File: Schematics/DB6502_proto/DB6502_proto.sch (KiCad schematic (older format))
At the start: 16 parts, among them U1 74AC32, U2 74HC21, U3 74AC74, U4 74AC04, U5 65C02S, U6 74AC08, U7 22V10C, U8 74AC138

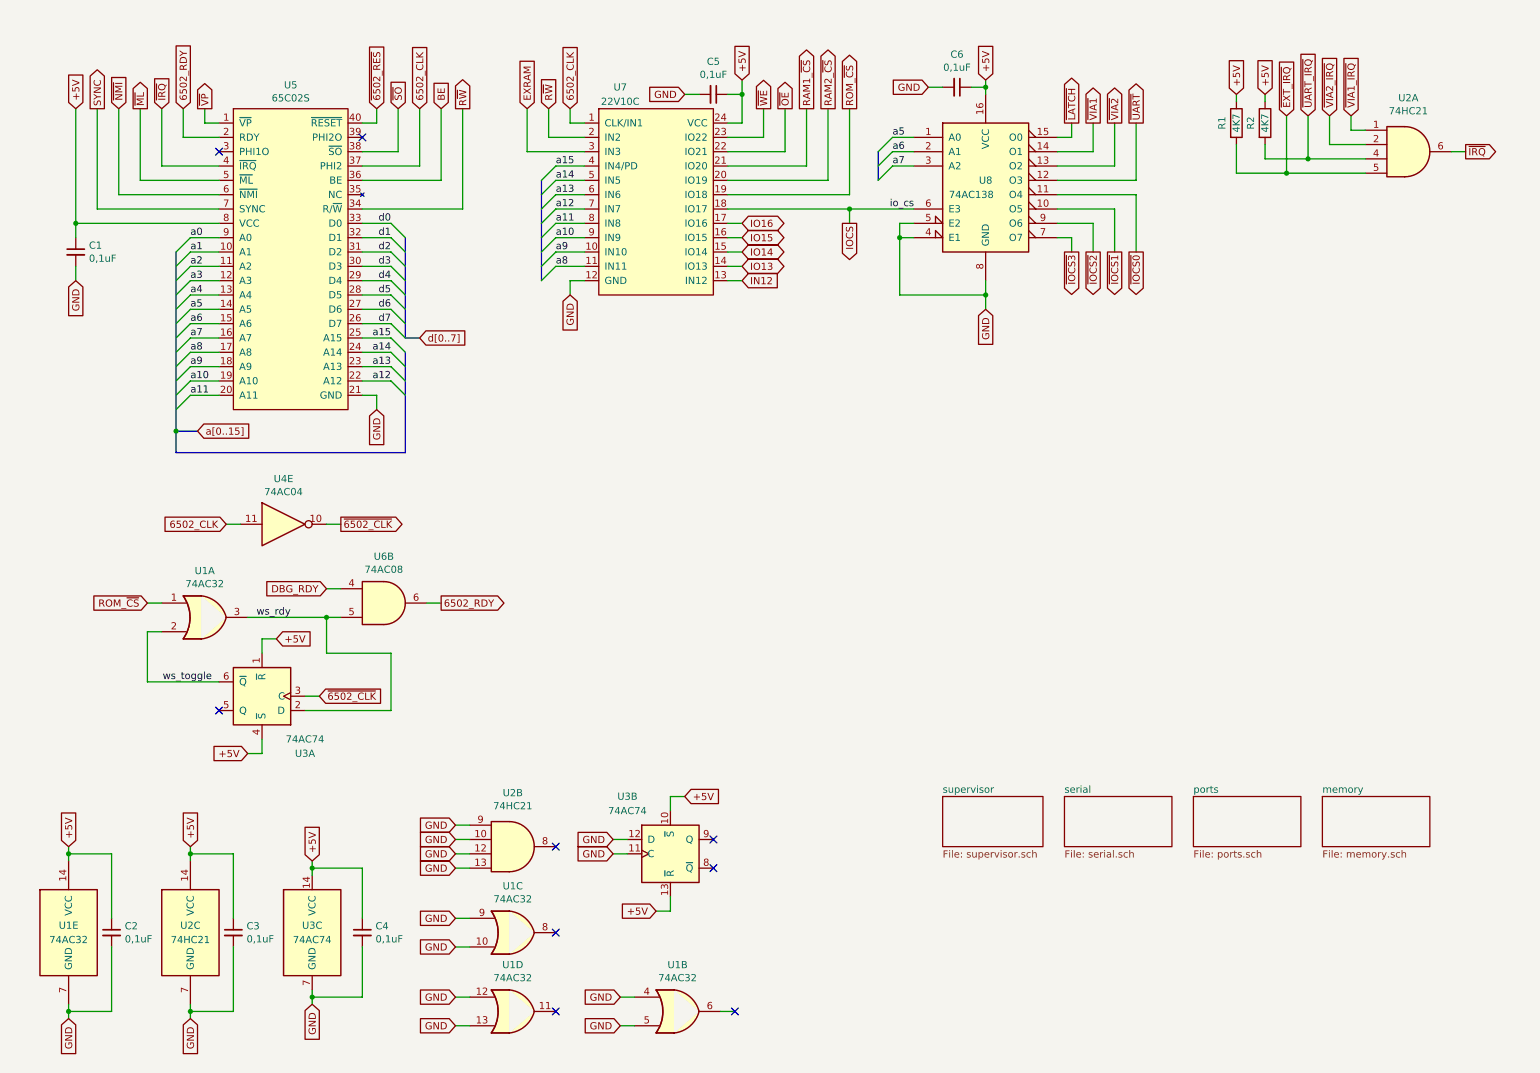
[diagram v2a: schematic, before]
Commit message: Rearranged global labels to make things neat
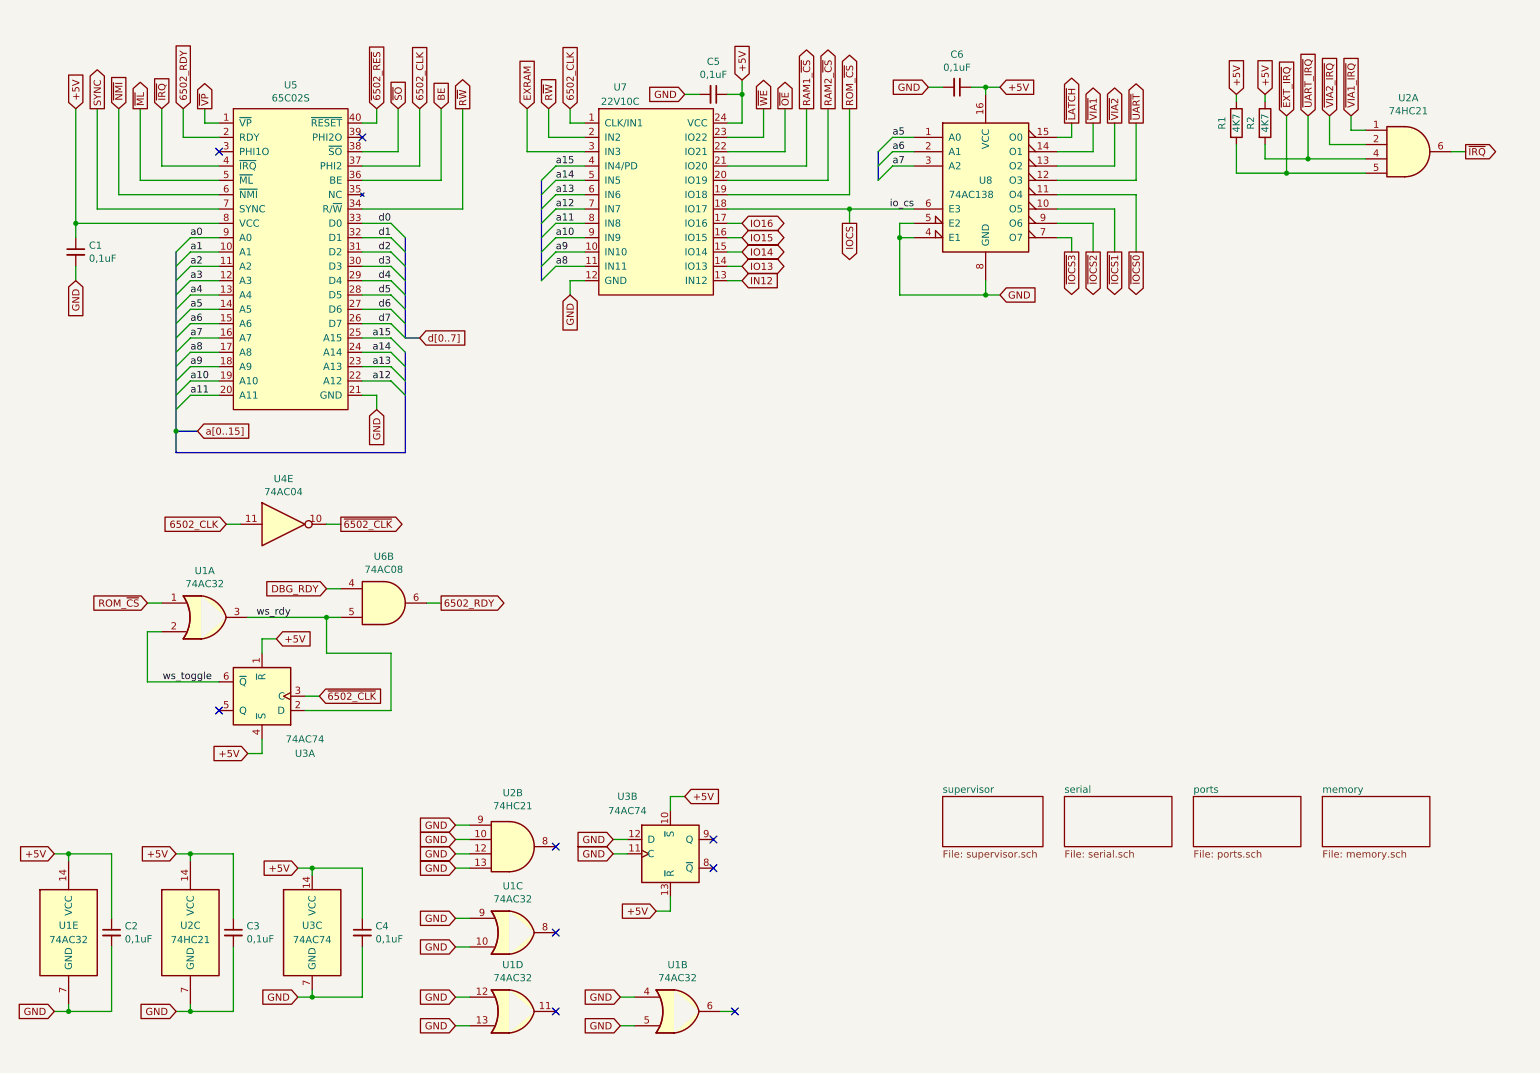
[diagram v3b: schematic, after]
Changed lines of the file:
@@
 Wire Wire Line
 	6600 1550 6750 1550
-Text GLabel 7250 950  1    50   Input ~ 0
-+5V
-Wire Wire Line
-	7250 950  7250 1000
-Text GLabel 7250 2550 3    50   Input ~ 0
-GND
-Wire Wire Line
-	7250 2550 7250 2450
+Text GLabel 7350 1000 2    50   Input ~ 0
++5V
+Wire Wire Line
+	7350 1000 7250 1000
+Text GLabel 7350 2450 2    50   Input ~ 0
+GND
+Wire Wire Line
+	7350 2450 7250 2450
 Wire Wire Line
 	7250 2450 6650 2450
@@
 	1    0    0    -1
 $EndComp
-Text GLabel 850  6300 1    50   Input ~ 0
-+5V
-Text GLabel 850  7500 3    50   Input ~ 0
-GND
-Wire Wire Line
-	850  6300 850  6350
-Wire Wire Line
-	850  7500 850  7450
+Text GLabel 750  6350 0    50   Input ~ 0
++5V
+Text GLabel 750  7450 0    50   Input ~ 0
+GND
+Wire Wire Line
+	750  6350 850  6350
+Wire Wire Line
+	750  7450 850  7450
 $Comp
 L Device:C_Small C2
@@
 	1    0    0    -1
 $EndComp
-Text GLabel 1700 6300 1    50   Input ~ 0
-+5V
-Text GLabel 1700 7500 3    50   Input ~ 0
-GND
-Wire Wire Line
-	1700 7500 1700 7450
+Text GLabel 1600 6350 0    50   Input ~ 0
++5V
+Text GLabel 1600 7450 0    50   Input ~ 0
+GND
+Wire Wire Line
+	1600 7450 1700 7450
 Wire Wire Line
 	1700 6400 1700 6350
@@
 Connection ~ 1700 6350
 Wire Wire Line
-	1700 6350 1700 6300
+	1700 6350 1600 6350
 Wire Wire Line
 	1700 7450 2000 7450
@@
 	1    0    0    -1
 $EndComp
-Text GLabel 2550 7400 3    50   Input ~ 0
-GND
-Wire Wire Line
-	2550 7400 2550 7350
-Text GLabel 2550 6400 1    50   Input ~ 0
-+5V
-Wire Wire Line
-	2550 6400 2550 6450
+Text GLabel 2450 7350 0    50   Input ~ 0
+GND
+Wire Wire Line
+	2450 7350 2550 7350
+Text GLabel 2450 6450 0    50   Input ~ 0
++5V
+Wire Wire Line
+	2450 6450 2550 6450
 $Comp
 L Device:C_Small C?

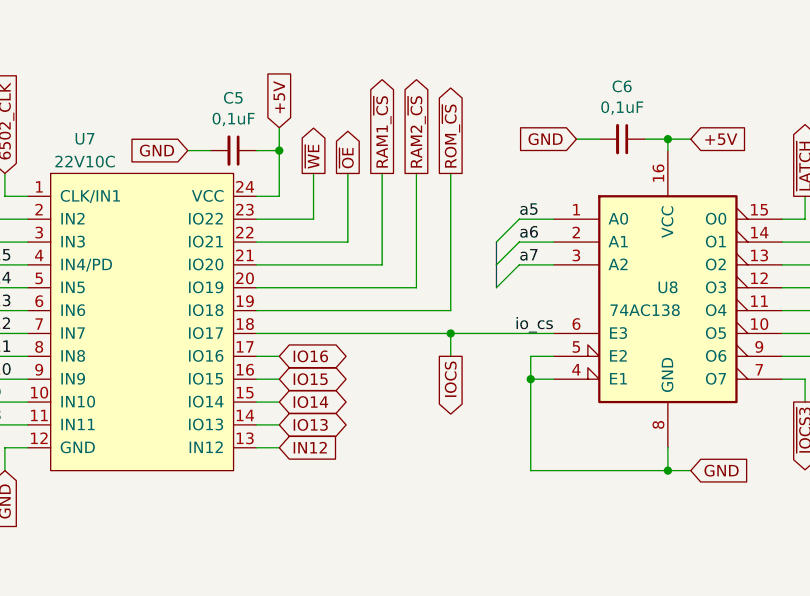
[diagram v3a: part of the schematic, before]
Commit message: Replaced nWE with nWR and nOE with nRD
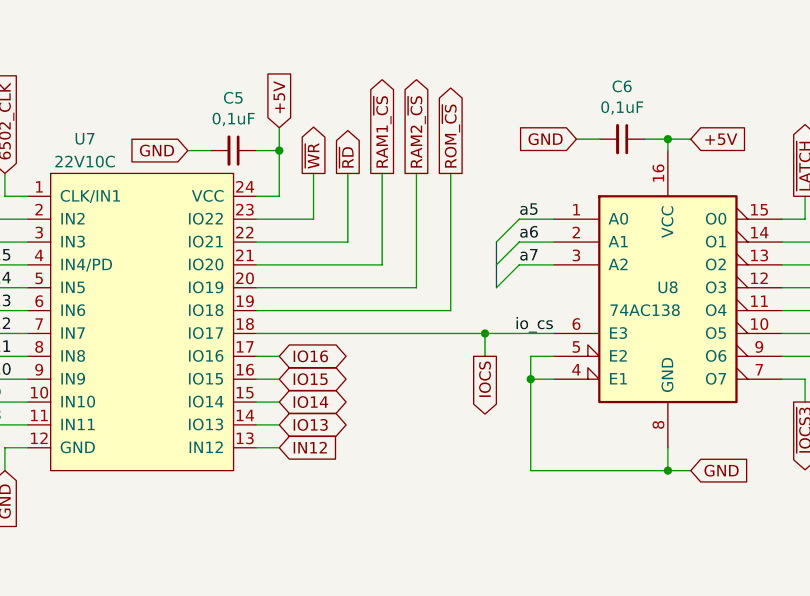
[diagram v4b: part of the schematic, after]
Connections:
- net ~OE renamed ~RD
- net ~WE renamed ~WR
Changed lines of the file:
@@
 	4050 1450 4450 1450
 Text GLabel 5700 1150 1    50   Output ~ 0
-~WE
+~WR
 Text GLabel 5850 1150 1    50   Output ~ 0
-~OE
+~RD
 Wire Wire Line
 	5700 1150 5700 1350
@@
 $EndSheet
 Wire Wire Line
-	5450 1850 6300 1850
+	5450 1850 6450 1850
 Text Label 6750 1850 2    50   ~ 0
 io_cs
-Text GLabel 6300 1950 3    50   Output ~ 0
+Text GLabel 6450 1950 3    50   Output ~ 0
 IOCS
 Wire Wire Line
-	6300 1950 6300 1850
-Connection ~ 6300 1850
-Wire Wire Line
-	6300 1850 6750 1850
+	6450 1950 6450 1850
+Connection ~ 6450 1850
+Wire Wire Line
+	6450 1850 6750 1850
 Wire Bus Line
 	6500 1450 6500 1650

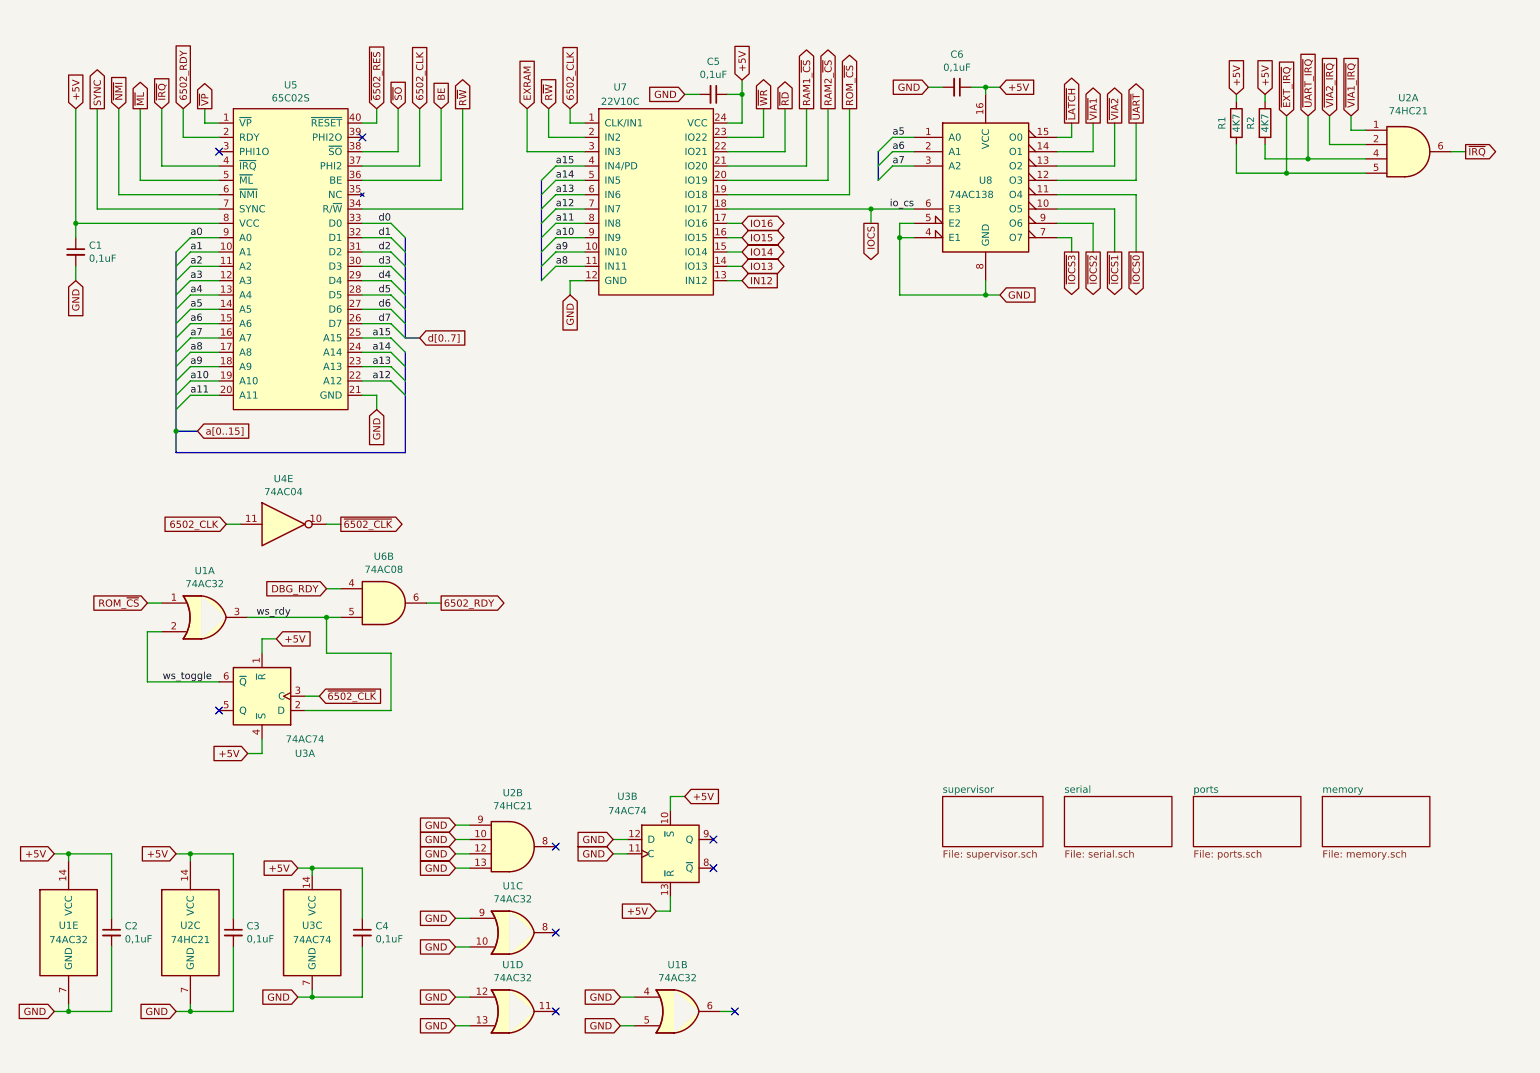
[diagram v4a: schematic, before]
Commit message: Updated schematic to reflect new wait state generator design
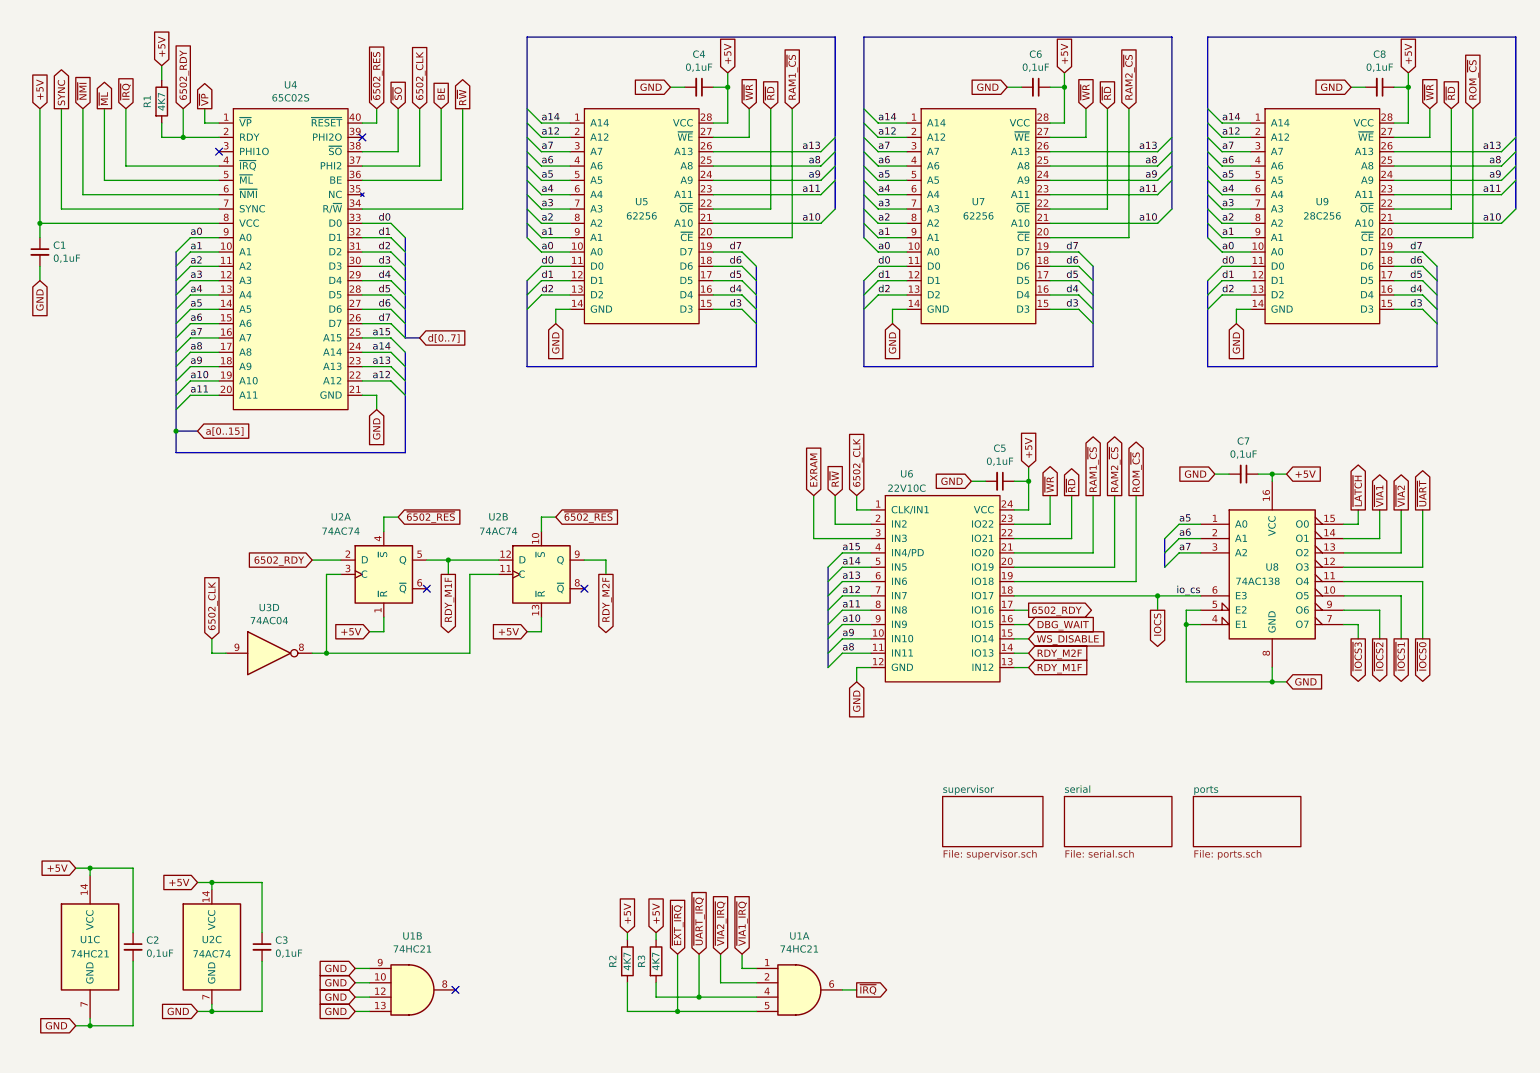
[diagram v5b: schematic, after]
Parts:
- removed C2: 0,1uF, Capacitor_THT:C_Disc_D5.0mm_W2.5mm_P2.50mm, symbol Device:C_Small
- removed U1: 74AC32, Package_DIP:DIP-14_W7.62mm_Socket, symbol 74xx:74LS32
- removed U6: 74AC08, Package_DIP:DIP-14_W7.62mm_Socket, symbol 74xx:74LS08
- added C4, C6, C8: 0,1uF, Capacitor_THT:C_Disc_D5.0mm_W2.5mm_P2.50mm, symbol Device:C_Small
- added R1: 4K7, Resistor_THT:R_Axial_DIN0207_L6.3mm_D2.5mm_P10.16mm_Horizontal, symbol Device:R
- added U5, U7: 62256, Package_DIP:DIP-28_W15.24mm_Socket, symbol 6502:62256
- added U9: 28C256, Package_DIP:DIP-28_W15.24mm_Socket, symbol 6502:28C256
- renumbered C3 to C2, C4 to C3, C6 to C7, R1 to R2, R2 to R3, U2 to U1, U3 to U2, U4 to U3, U5 to U4, U7 to U6
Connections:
- net IN12 is gone; now on net RDY_M1F: U6.13 (IN12)
- net IO13 is gone; now on net RDY_M2F: U6.14 (IO13)
- net IO16 is gone; now on net 6502_RDY: U6.17 (IO16)
- net ws_rdy is gone; now on net 6502_RDY: U2.2 (D)
- net +5V: now also C4.1, C6.1, C8.1, R1.1, U5.28 (VCC), U7.28 (VCC), U9.28 (VCC); no longer U2.10 (~S), U2.4 (~S)
- net 6502_CLK: now also U3.9; no longer U3.11
- net 6502_RDY: now also R1.2
- net GND: now also C4.2, C6.2, C8.2, U5.14 (GND), U7.14 (GND), U9.14 (GND); no longer U2.11 (C), U2.12 (D)
- net RAM1_~CS: now also U5.20 (~CE)
- net RAM2_~CS: now also U7.20 (~CE)
- net ROM_~CS: now also U9.20 (~CE)
- net a0: now also U5.10 (A0), U7.10 (A0), U9.10 (A0)
- net a1: now also U5.9 (A1), U7.9 (A1), U9.9 (A1)
- net a10: now also U5.21 (A10), U7.21 (A10), U9.21 (A10)
- net a11: now also U5.23 (A11), U7.23 (A11), U9.23 (A11)
- net a12: now also U5.2 (A12), U7.2 (A12), U9.2 (A12)
- net a13: now also U5.26 (A13), U7.26 (A13), U9.26 (A13)
- net a14: now also U5.1 (A14), U7.1 (A14), U9.1 (A14)
- net a2: now also U5.8 (A2), U7.8 (A2), U9.8 (A2)
- net a3: now also U5.7 (A3), U7.7 (A3), U9.7 (A3)
- net a4: now also U5.6 (A4), U7.6 (A4), U9.6 (A4)
- net a5: now also U5.5 (A5), U7.5 (A5), U9.5 (A5)
- net a6: now also U5.4 (A6), U7.4 (A6), U9.4 (A6)
- net a7: now also U5.3 (A7), U7.3 (A7), U9.3 (A7)
- net a8: now also U5.25 (A8), U7.25 (A8), U9.25 (A8)
- net a9: now also U5.24 (A9), U7.24 (A9), U9.24 (A9)
- net d0: now also U5.11 (D0), U7.11 (D0), U9.11 (D0)
- net d1: now also U5.12 (D1), U7.12 (D1), U9.12 (D1)
- net d2: now also U5.13 (D2), U7.13 (D2), U9.13 (D2)
- net d3: now also U5.15 (D3), U7.15 (D3), U9.15 (D3)
- net d4: now also U5.16 (D4), U7.16 (D4), U9.16 (D4)
- net d5: now also U5.17 (D5), U7.17 (D5), U9.17 (D5)
- net d6: now also U5.18 (D6), U7.18 (D6), U9.18 (D6)
- net d7: now also U5.19 (D7), U7.19 (D7), U9.19 (D7)
- net ~6502_RES: now also U2.10 (~S), U2.4 (~S)
- net ~RD: now also U5.22 (~OE), U7.22 (~OE), U9.22 (~OE)
- net ~WR: now also U5.27 (~WE), U7.27 (~WE), U9.27 (~WE)
- net RDY_M1F: now reaches U2.5 (Q)
- net RDY_M1F: now also U2.12 (D)
- net RDY_M2F: now reaches U2.9 (Q)
- net IO14 renamed WS_DISABLE
- net IO15 renamed DBG_WAIT
- net ws_toggle: no longer names the net of U2.6 (~Q)
- net ~6502_CLK: no longer names the net of U2.3 (C)
- net ~6502_CLK: now also U2.11 (C), U3.8; no longer U3.10
- no-connect marks 9 -> 5
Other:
- moved on the sheet: C1, C2, C3, C5, C7, R2, R3, U1A, U1B, U1C, U2A, U2B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
